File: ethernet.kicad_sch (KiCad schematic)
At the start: 1 part, among them U1 W5500

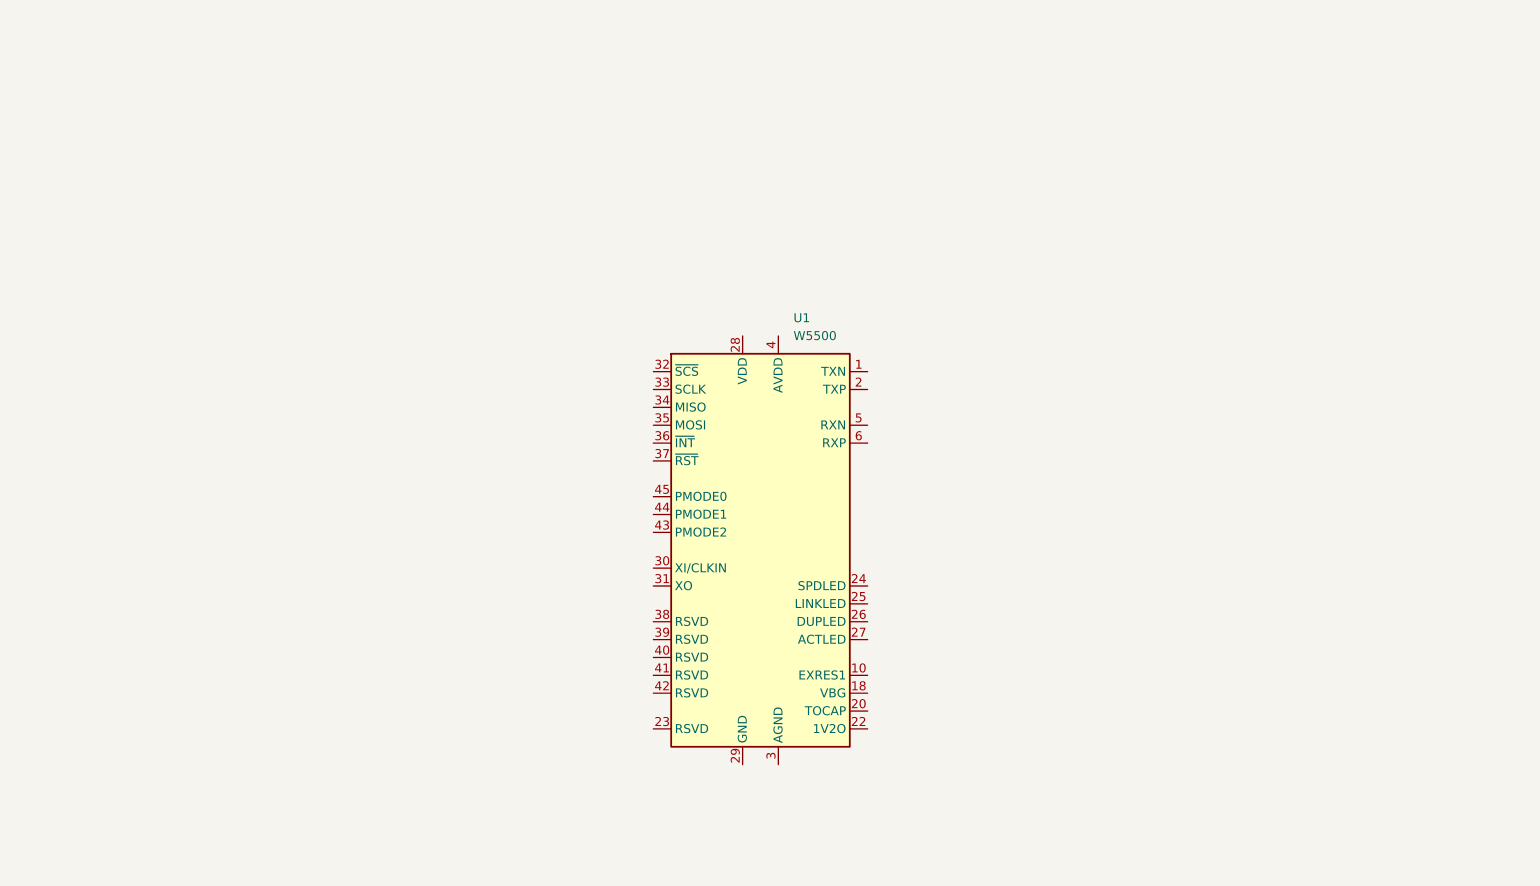
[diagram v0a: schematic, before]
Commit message: added ethernet phy
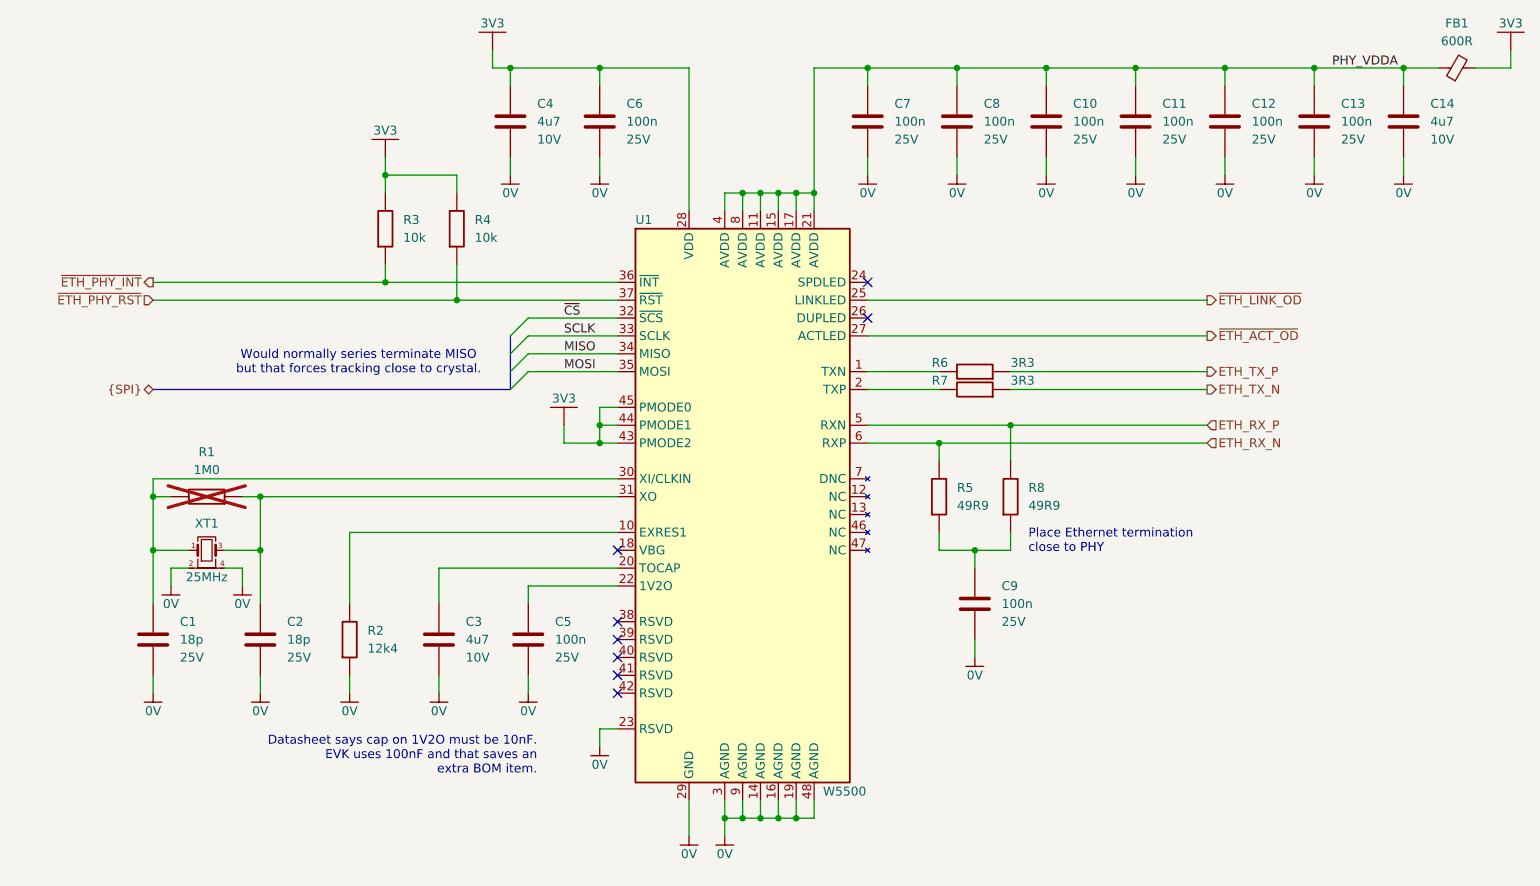
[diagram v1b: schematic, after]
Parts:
- added C1, C2: 18p, Capacitor_WUT:C_0402_1005Metric, symbol capacitor_auto_wut:Kemet C0402C180K3GACTU
- added C10, C11, C12, C13, C5, C6, C7, C8, C9: 100n, Capacitor_WUT:C_0402_1005Metric, symbol aaa_capacitor_auto_wut:Yageo CC0402KRX7R8BB104
- added C14, C3, C4: 4u7, Capacitor_WUT:C_0402_1005Metric, symbol capacitor_auto_wut:Murata GRM155D71A475ME15
- added FB1: 600R, Inductor_SMD:L_0603_1608Metric, symbol aaa_ferrite_bead_auto_wut:Murata BLM18AG601SN1D
- added R1: 1M0, Resistor_WUT:R_0402_1005Metric, symbol resistor_auto_wut:KOA Speer RK73H1ETTP1004F
- added R2: 12k4, Resistor_WUT:R_0402_1005Metric, symbol resistor_auto_wut:KOA Speer RK73H1ETTP1242F
- added R3, R4: 10k, Resistor_WUT:R_0402_1005Metric, symbol aaa_resistor_auto_wut:KOA Speer RK73H1ETTP1002F
- added R5, R8: 49R9, Resistor_WUT:R_0402_1005Metric, symbol resistor_auto_wut:KOA Speer RK73H1ETTP49R9F
- added R6, R7: 3R3, Resistor_WUT:R_0402_1005Metric, symbol resistor_auto_wut:KOA Speer RK73H1ETTP3R30F
- added XT1: 25MHz, Crystal_WUT:Murata_XRCGB, symbol Crystal_WUT:Murata_XRCGB25M000F3M18R0
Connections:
- net at U1.1 (TXN): now also R6.1
- net at U1.10 (EXRES1): now also R2.1
- net PHY_VDDA: now reaches U1.11 (AVDD), U1.15 (AVDD), U1.17 (AVDD), U1.21 (AVDD), U1.4 (AVDD), U1.8 (AVDD)
- net PHY_VDDA: now also C10.1, C11.1, C12.1, C13.1, C14.1, C7.1, C8.1, FB1.1
- net 0V: now reaches U1.14 (AGND), U1.16 (AGND), U1.19 (AGND), U1.3 (AGND), U1.48 (AGND), U1.9 (AGND)
- net 0V: now also U1.23 (RSVD), U1.29 (GND), C1.2, C10.2, C11.2, C12.2, C13.2, C14.2, C2.2, C3.2, C4.2, C5.2, C6.2, C7.2, C8.2, C9.2, R2.2, XT1.2, XT1.4
- net at U1.2 (TXP): now also R7.1
- net at U1.20 (TOCAP): now also C3.1
- net at U1.22 (1V2O): now also C5.1
- net ~{ETH_LINK_OD}: now reaches U1.25 (LINKLED)
- net ~{ETH_ACT_OD}: now reaches U1.27 (ACTLED)
- net 3V3: now reaches U1.28 (VDD)
- net 3V3: now also U1.43 (PMODE2), U1.44 (PMODE1), U1.45 (PMODE0), C4.1, C6.1, FB1.2, R3.1, R4.1
- net at U1.30 (XI/CLKIN): now also C1.1, R1.1, XT1.1
- net at U1.31 (XO): now also C2.1, R1.2, XT1.3
- net ~{CS}: now reaches U1.32 (~{SCS})
- net SCLK: now reaches U1.33 (SCLK)
- net MISO: now reaches U1.34 (MISO)
- net MOSI: now reaches U1.35 (MOSI)
- net ~{ETH_PHY_INT}: now reaches U1.36 (~{INT})
- net ~{ETH_PHY_INT}: now also R3.2
- net ~{ETH_PHY_RST}: now reaches U1.37 (~{RST})
- net ~{ETH_PHY_RST}: now also R4.2
- net ETH_RX_P: now reaches U1.5 (RXN)
- net ETH_RX_P: now also R8.1
- net ETH_RX_N: now reaches U1.6 (RXP)
- net ETH_RX_N: now also R5.1
- new net: C9.1, R5.2, R8.2
- new net ETH_TX_N: R7.2
- new net ETH_TX_P: R6.2
- no-connect marks 0 -> 8
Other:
- note added: "Datasheet says cap on 1V2O must be 10nF. EVK uses 100nF and that saves an extra BOM item."
- note added: "Place Ethernet termination close to PHY"
- note added: "Would normally series terminate MISO but that forces tracking close to crystal."

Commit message: started on mcu pinout
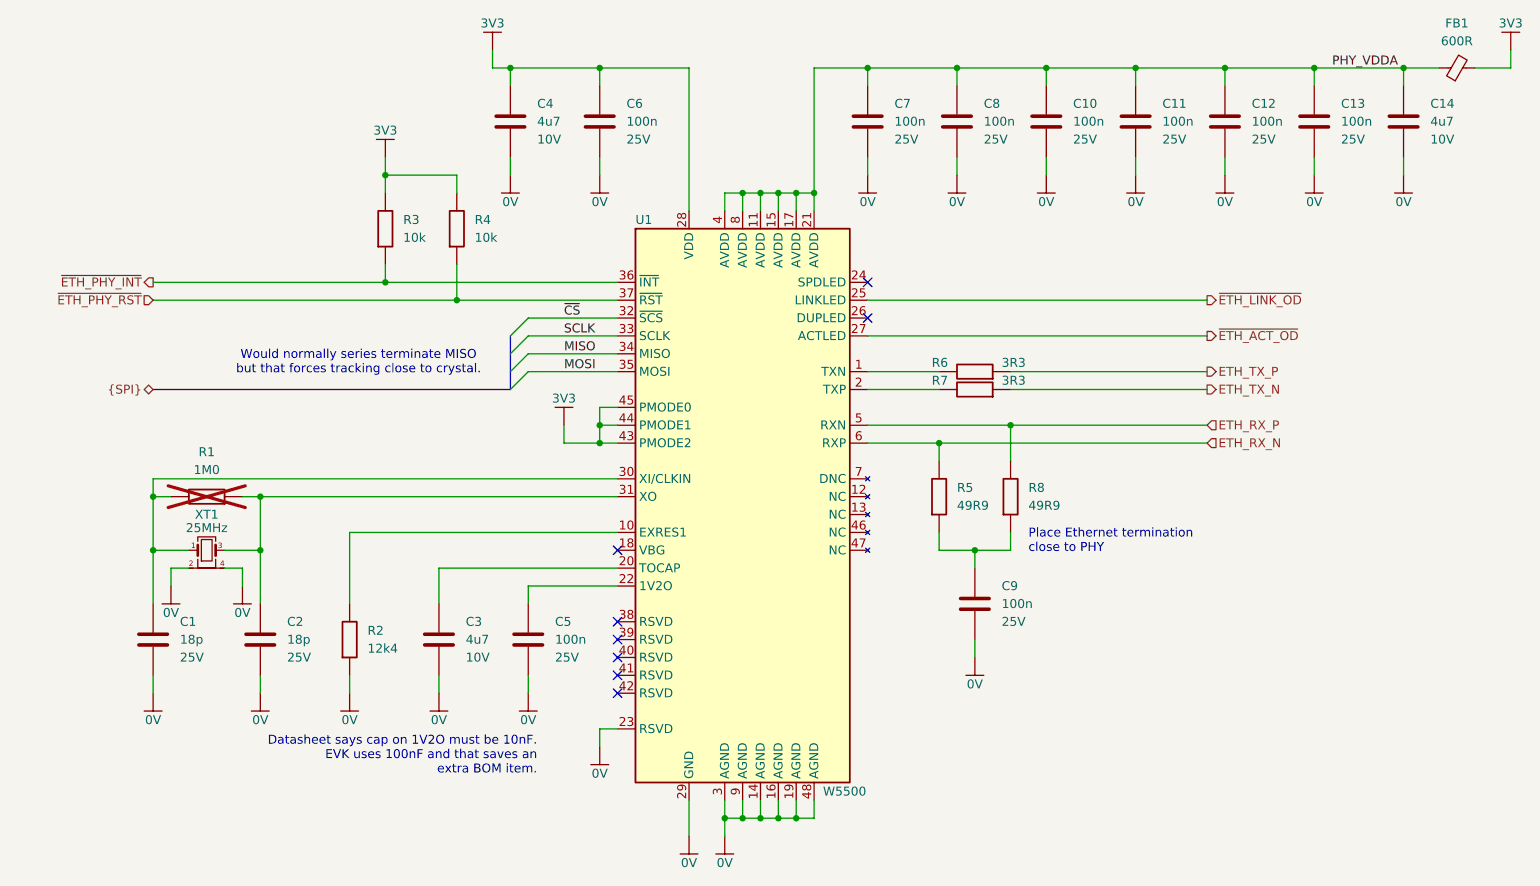
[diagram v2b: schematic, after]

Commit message: more progress
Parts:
- removed R4: 10k, Resistor_WUT:R_0402_1005Metric, symbol aaa_resistor_auto_wut:KOA Speer RK73H1ETTP1002F
